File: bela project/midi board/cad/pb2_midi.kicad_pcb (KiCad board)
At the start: 2 copper layers, 44 x 40 mm, 15 parts, among them J1 MIDI_IN, J2 MIDI_OUT, J3 RIBBON, U2 H11L1M

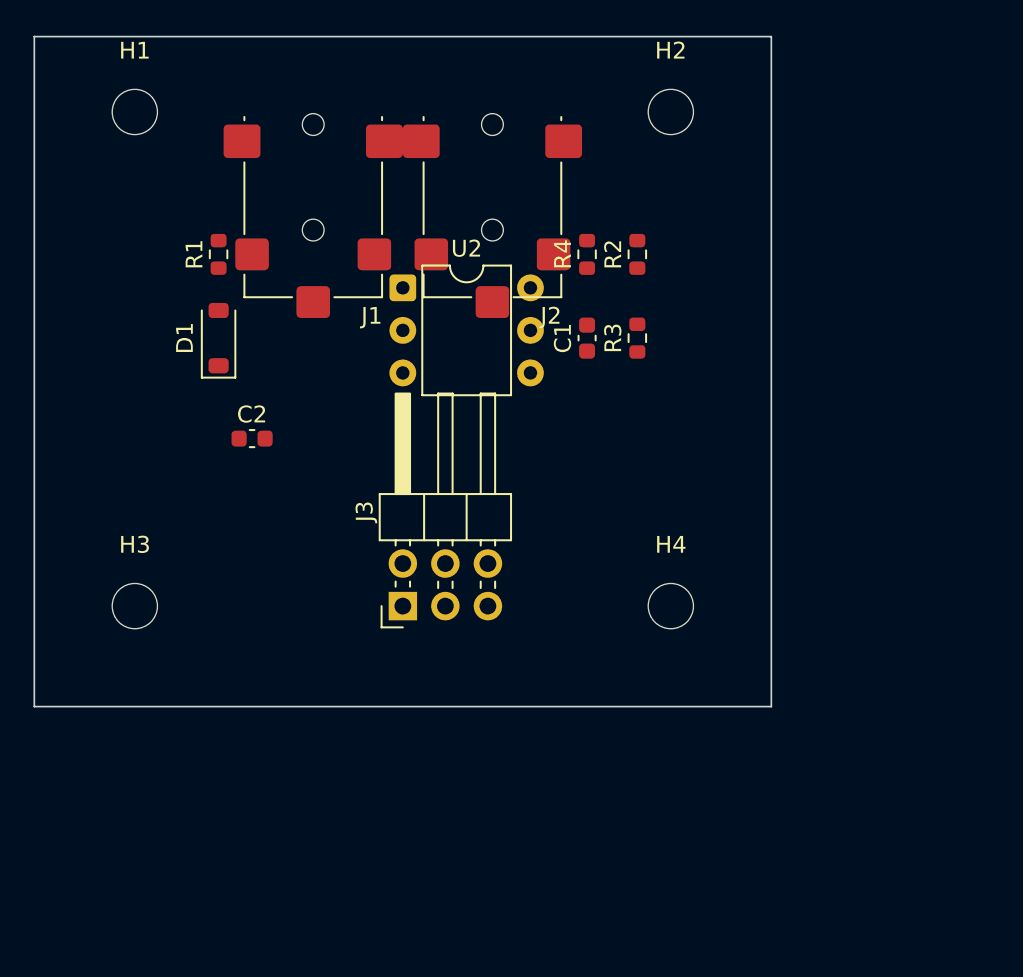
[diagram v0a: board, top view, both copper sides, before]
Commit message: MIDI board: add panel-aligned power on/off button (SW1) + soft-power header
Add an Alps SKRTLAE010 side-actuated SMD power button in the same panel row as
the jacks, 10.7mm from the last MIDI jack, actuator co-planar with the jack
fronts (X=60.6) and at the same lifted height. Soft-power to the Beagle via a
new 1x3 header J4 (PWR_BTN/GND/3V3), conditioned with R5 (10k pull-up) + C3
(100n debounce). Aligned assembly STEP now shows the button + its panel hole.

Also: net application now sets all pads sharing a number (SW1 has two "1" pads);
board re-laid to 57x46mm (Lumberg pads span ~10mm in Y). BOM + README updated.

Co-Authored-By: Claude Opus 4.8 (1M context) <noreply@anthropic.com>
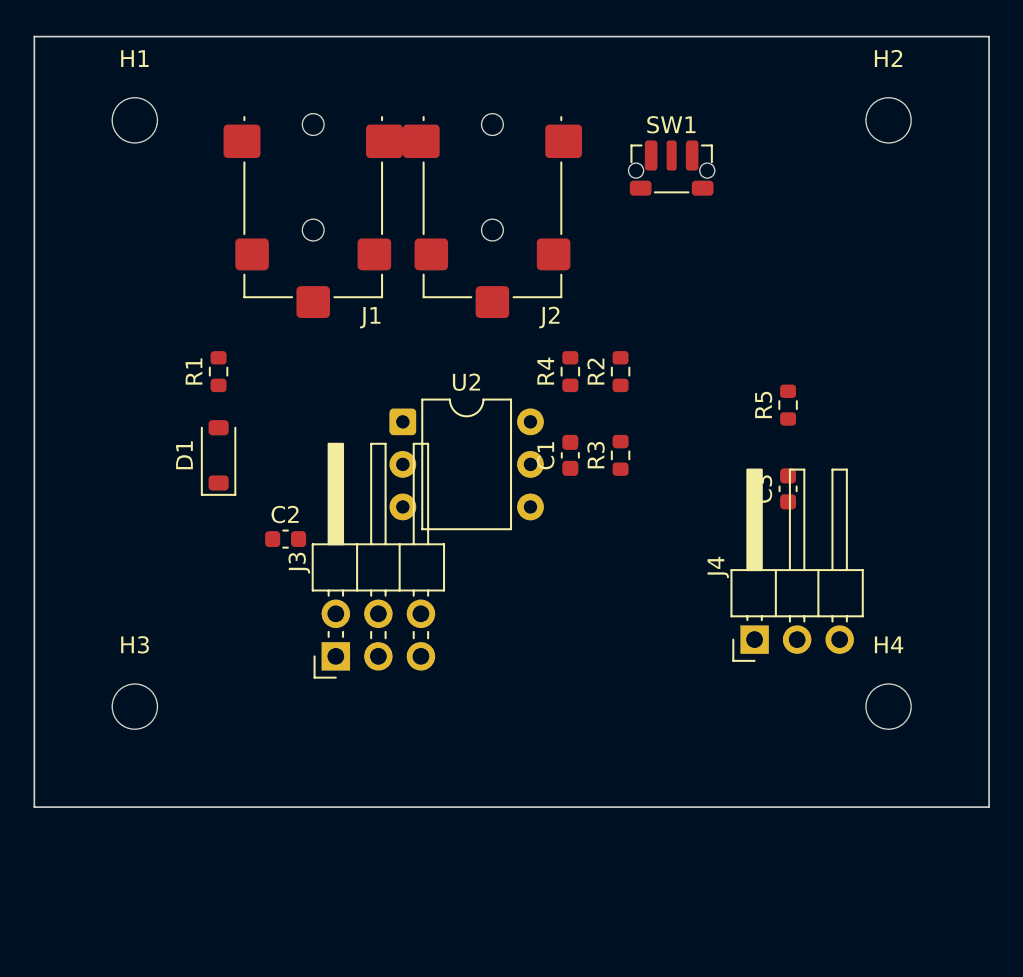
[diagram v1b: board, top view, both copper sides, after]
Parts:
- added C3: 100n, C_0603_1608Metric, F.Cu at (43.0, 27.0)
- added J4: PWR_HDR, PinHeader_1x03_P2.54mm_Horizontal, F.Cu at (41.0, 36.0)
- added R5: 10k, R_0603_1608Metric, F.Cu at (43.0, 22.0)
- added SW1: PWR, SW_Push_1P1T-MP_NO_Horizontal_Alps_SKRTLAE010, F.Cu at (36.0, 8.00)
- moved H4 14.3 mm to (49.0, 40.0)
- moved H2 13.0 mm to (49.0, 5.00)
- moved U2 8.00 mm to (20.0, 23.0)
- moved C1 7.07 mm to (30.0, 25.0)
- moved R2 7.07 mm to (33.0, 20.0)
- moved R3 7.07 mm to (33.0, 25.0)
- moved R4 7.07 mm to (30.0, 20.0)
- moved D1 7.00 mm to (9.00, 25.0)
- moved R1 7.00 mm to (9.00, 20.0)
- moved C2 6.32 mm to (13.0, 30.0)
- moved H3 6.00 mm to (4.00, 40.0)
- moved J3 5.00 mm to (16.0, 37.0)
- moved H1 0.50 mm to (4.00, 5.00)
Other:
- board size 44 x 40 mm -> 57 x 46 mm

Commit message: MIDI board: route (Freerouting) + GND plane + DRC cleanup
Routed the board with Freerouting 2.2.4 (2-layer, both F/B signal, clearance
0.15) and poured a GND plane on F.Cu + B.Cu with solid pad connection.
Result: routing_complete, 0 unconnected, 0 DRC errors, 2 vias.

DRC cleanup: shrank the conservative KiCad courtyards (jacks fit 10.7mm as on
the Bela; Lumberg/switch MP pads trimmed), dropped footprint silkscreen graphics,
AISLER hole clearances. Added route_export_dsn.py / route_import_ses.py + the
DSN/SES + routed renders. One residual cosmetic silk-over-copper (C1 ref).

Also hardened gen_pcb: net-apply over all pads sharing a number, and footprint
edits before b.Add (SWIG handles go stale / segfault after Add).

Co-Authored-By: Claude Opus 4.8 (1M context) <noreply@anthropic.com>
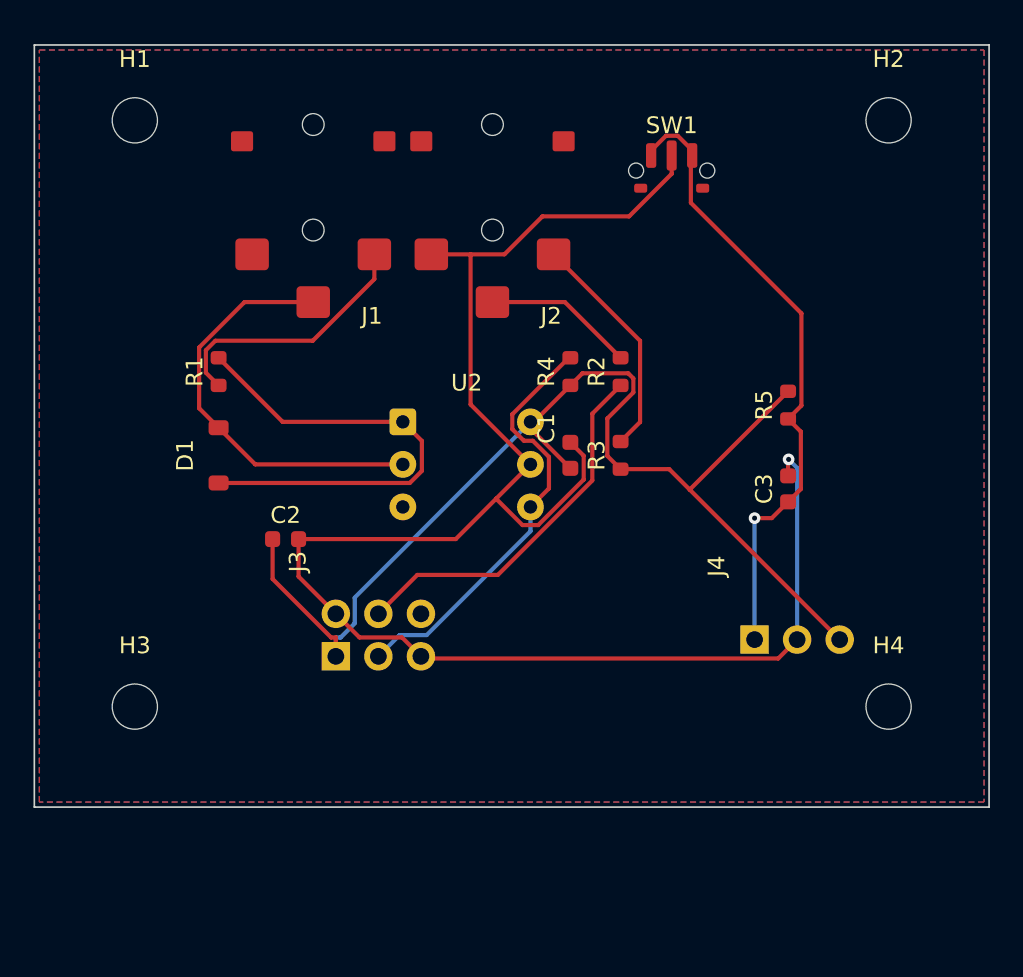
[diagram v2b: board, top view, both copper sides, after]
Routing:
- net GND: track 0.00 -> 103.2 mm, vias 0 -> 1
- net +3V3: track 0.00 -> 70.8 mm
- net PWR_BTN: track 0.00 -> 37.8 mm, vias 0 -> 1
- net MIDI_IN_A: track 0.00 -> 28.4 mm
- net UART_RX: track 0.00 -> 25.7 mm
- net MIDI_IN_K: track 0.00 -> 25.1 mm
- net UART_TX: track 0.00 -> 22.4 mm
- net MIDI_IN_RING: track 0.00 -> 15.7 mm
- net MIDI_OUT_RING: track 0.00 -> 13.8 mm
- net MIDI_OUT_TIP: track 0.00 -> 9.03 mm
- added copper zone on B.Cu, net GND
- added copper zone on F.Cu, net GND
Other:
- board size 57 x 46 mm -> 57 x 45.5 mm

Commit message: MIDI board fix: J3/J4 headers collided with the opto U2 in 3D — reoriented + re-routed
The right-angle ribbon/power headers (J3, J4) pointed INTO the board (pins toward
U2), overlapping the optocoupler body in 3D — the shrunk courtyards had let it pass
DRC. Restored full header courtyards (so DRC catches it), flipped J3/J4 to 270deg so
their pins exit the sandwich edge (away from U2), re-ran Freerouting + GND pour.
Result: no collision, 0 unconnected, 0 DRC errors. (Renders/book to be refreshed later.)

Co-Authored-By: Claude Opus 4.8 (1M context) <noreply@anthropic.com>
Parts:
- moved J4 2.00 mm to (41.0, 38.0), turned to -90 degrees
- moved J3 1.00 mm to (16.0, 38.0), turned to -90 degrees
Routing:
- net +3V3: track 70.8 -> 83.2 mm, vias 0 -> 1
- net MIDI_IN_A: track 28.4 -> 17.9 mm
- net UART_TX: track 22.4 -> 30.0 mm, vias 0 -> 1
- net MIDI_IN_K: track 25.1 -> 30.2 mm
- net GND: track 103.2 -> 100.0 mm, vias 1 -> 0
- net UART_RX: track 25.7 -> 28.8 mm, vias 0 -> 1
- net PWR_BTN: track 37.8 -> 38.9 mm, vias 1 -> 0
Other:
- board size 57 x 45.5 mm -> 57 x 53.6 mm
